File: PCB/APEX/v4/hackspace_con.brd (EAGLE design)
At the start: 73.7 x 26.7 mm, 13 parts

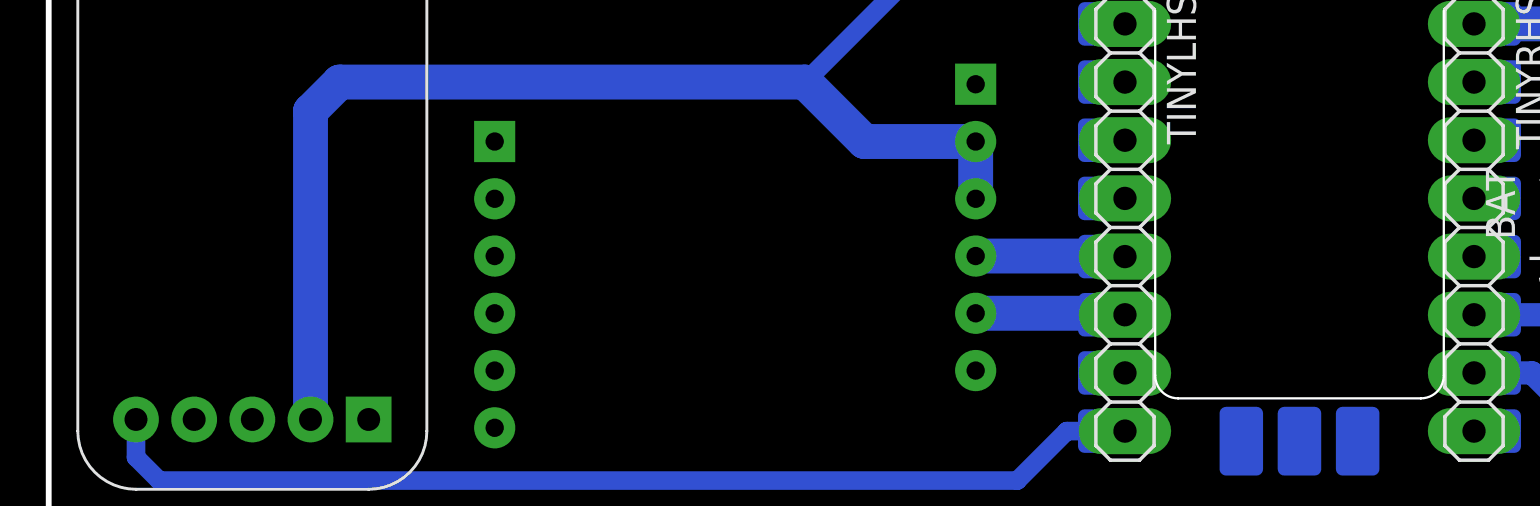
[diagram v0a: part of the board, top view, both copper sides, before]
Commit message: add labels
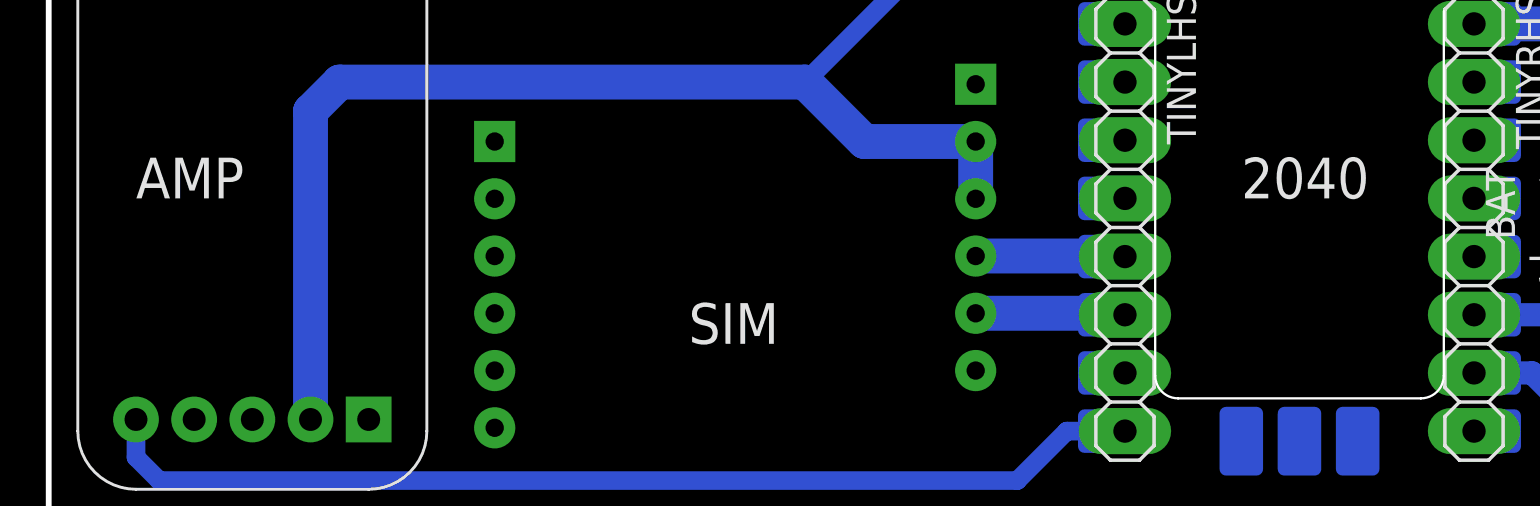
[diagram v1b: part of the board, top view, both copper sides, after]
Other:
- board text added: "2040"
- board text added: "AMP"
- board text added: "SIM"

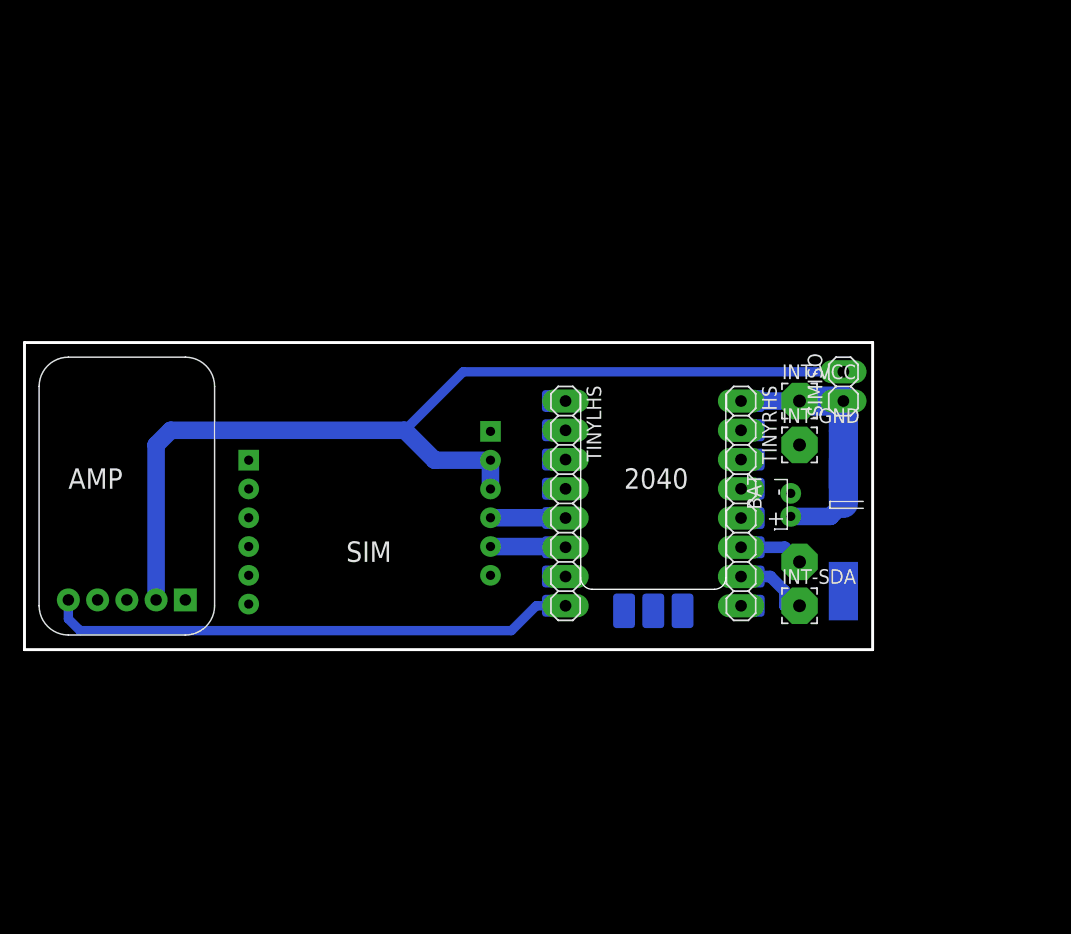
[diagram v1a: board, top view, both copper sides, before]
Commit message: flip installation orientation
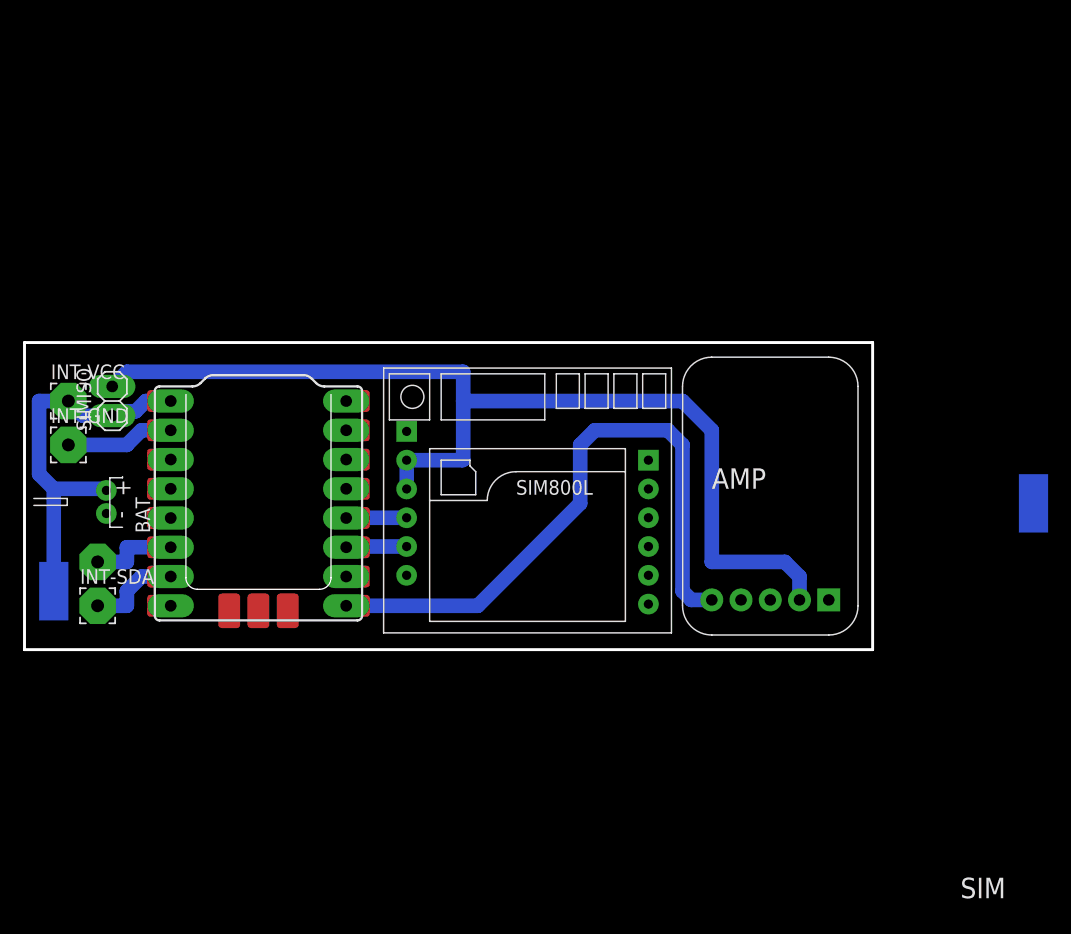
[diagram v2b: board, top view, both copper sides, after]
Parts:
- moved EXTV+ 69.5 mm to (-17.8, -52.1)
- moved SIMISO 63.5 mm to (-12.7, -35.6)
- moved INT-GND 63.5 mm to (-16.5, -39.4)
- moved INT-VCC 63.5 mm to (-16.5, -35.6)
- moved INT-SCL 61.0 mm to (-14.0, -49.5)
- moved INT-SDA 61.0 mm to (-14.0, -53.3)
- moved BAT 59.4 mm to (-13.2, -44.3), turned to 90 degrees
- moved JP2 55.9 mm to (44.5, -52.8)
- moved TINYRHS 49.5 mm to (-7.62, -44.5), flipped to the bottom
- moved A1 34.3 mm to (0.00, -34.3), flipped to the top
- moved TINYLHS 19.1 mm to (7.62, -44.5), flipped to the bottom
- moved EXTGND 18.2 mm to (67.3, -44.5)
- moved U$1 13.7 mm to (23.4, -44.2), flipped to the top
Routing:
- net VCC: track 19.7 -> 34.1 mm
- net GND: track 0.00 -> 9.42 mm
- net AIN+: track 45.6 -> 54.6 mm
- net SIMPOW: track 86.8 -> 90.3 mm
- net SCL: track 5.06 -> 7.62 mm
- net SDA: track 6.62 -> 8.15 mm
- net TX: track 5.99 -> 5.37 mm

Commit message: remove 2040 footprint
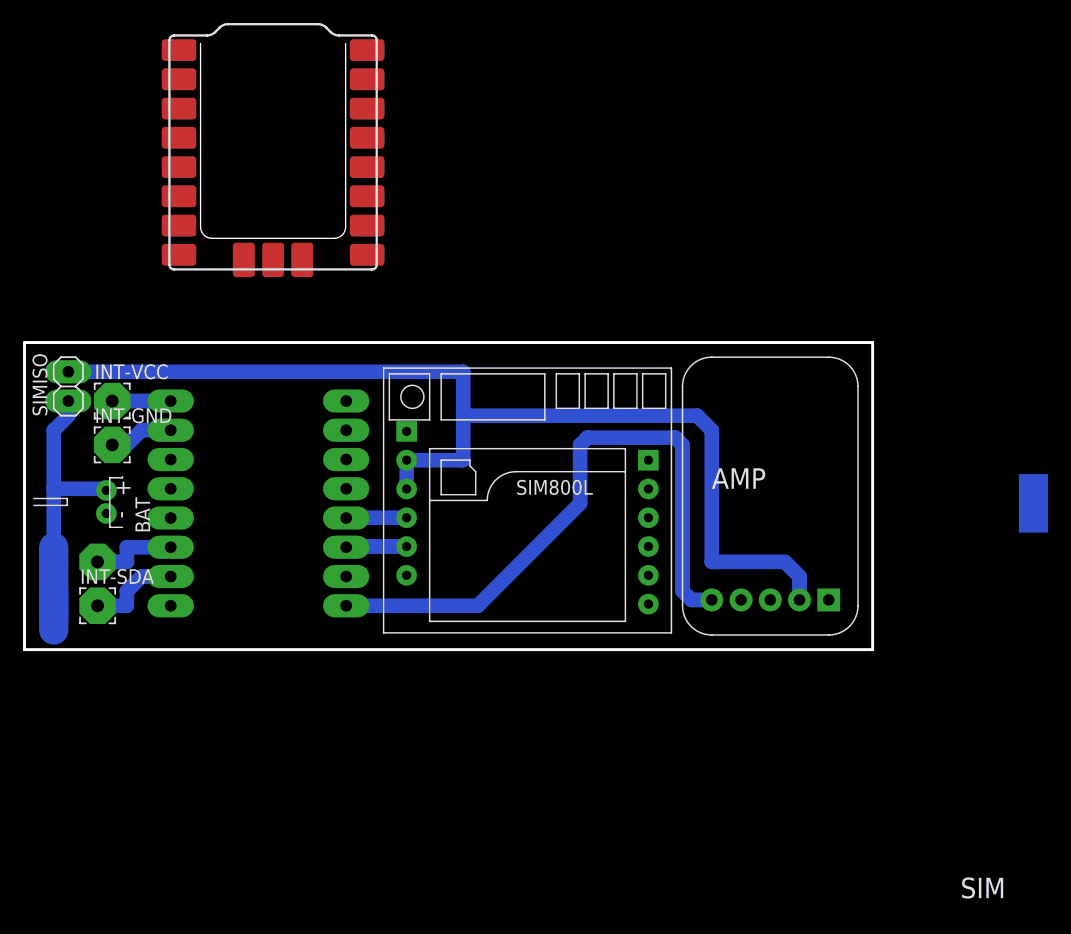
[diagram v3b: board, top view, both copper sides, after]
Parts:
- moved A1 30.5 mm to (1.27, -3.81)
- moved SIMISO 4.02 mm to (-16.5, -34.3)
- moved INT-GND 3.81 mm to (-12.7, -39.4)
- moved INT-VCC 3.81 mm to (-12.7, -35.6)
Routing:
- net GND: track 9.42 -> 4.34 mm
- net VCC: track 34.1 -> 30.1 mm
- net SIMPOW: track 90.3 -> 93.1 mm
- net AIN+: track 54.6 -> 54.1 mm

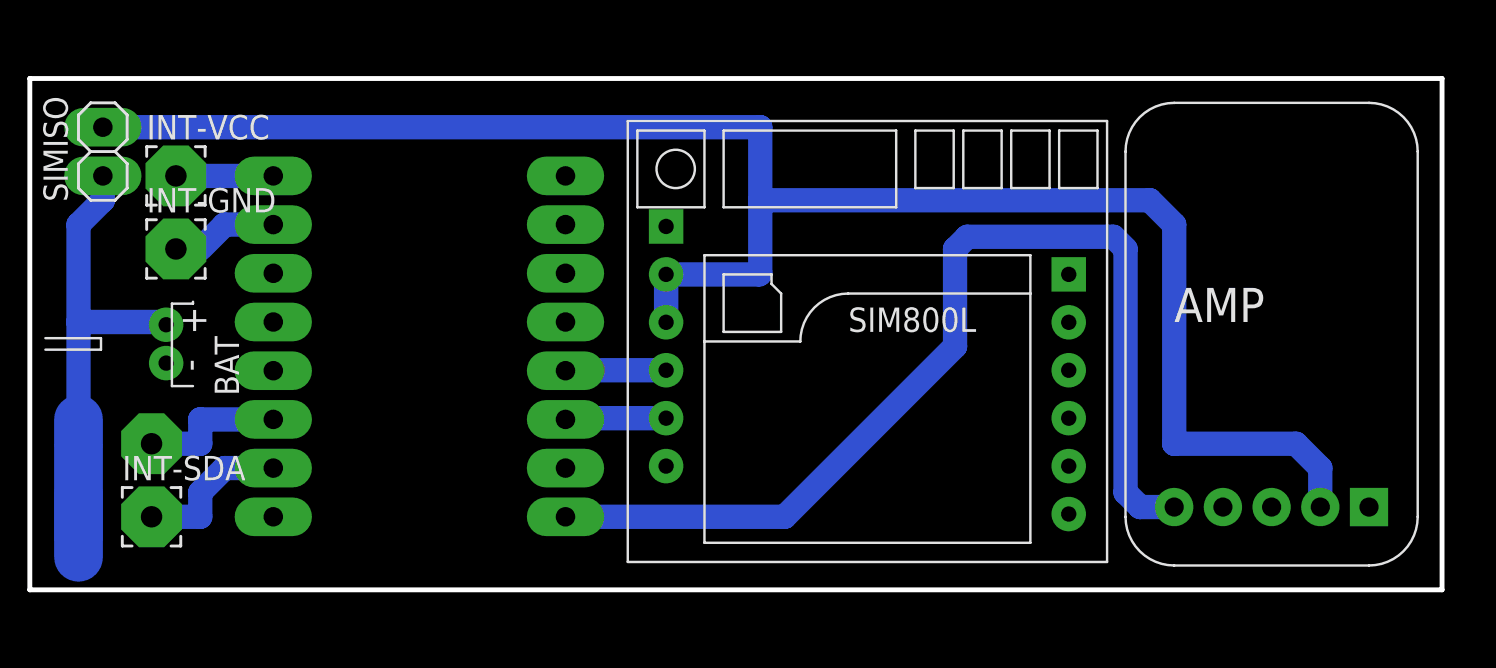
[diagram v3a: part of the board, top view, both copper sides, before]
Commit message: thiccer traces
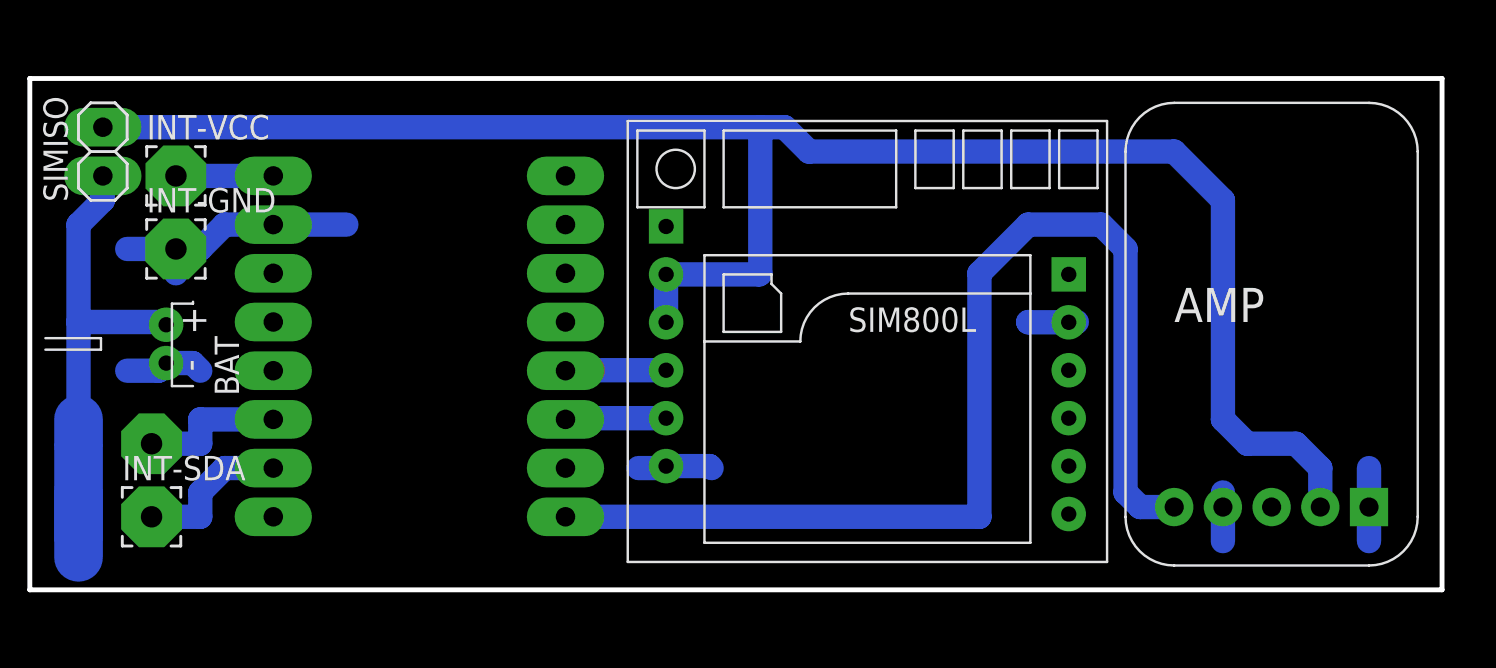
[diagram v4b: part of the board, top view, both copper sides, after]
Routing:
- net GND: track 4.34 -> 30.2 mm
- net AIN+: track 54.1 -> 59.0 mm
- net SIMPOW: track 93.1 -> 94.6 mm
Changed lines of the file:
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@@
 </polygon>
 <wire x1="-11.43" y1="-39.37" x2="-10.16" y2="-38.1" width="1.27" layer="16"/>
-<wire x1="-10.16" y1="-38.1" x2="-7.62" y2="-38.1" width="1.27" layer="16"/>
+<wire x1="41.91" y1="-52.07" x2="41.91" y2="-52.832" width="1.27" layer="16"/>
+<wire x1="41.91" y1="-52.832" x2="41.91" y2="-54.61" width="1.27" layer="16"/>
+<wire x1="49.53" y1="-50.8" x2="49.53" y2="-52.832" width="1.27" layer="16"/>
+<wire x1="49.53" y1="-52.832" x2="49.53" y2="-54.61" width="1.27" layer="16"/>
+<wire x1="12.868" y1="-50.696" x2="15.136" y2="-50.696" width="1.27" layer="16"/>
+<wire x1="15.136" y1="-50.696" x2="15.24" y2="-50.8" width="1.27" layer="16"/>
+<wire x1="12.868" y1="-50.696" x2="12.764" y2="-50.8" width="1.27" layer="16"/>
+<wire x1="12.764" y1="-50.8" x2="11.43" y2="-50.8" width="1.27" layer="16"/>
+<wire x1="-13.208" y1="-45.323" x2="-13.605" y2="-45.72" width="1.27" layer="16"/>
+<wire x1="-13.605" y1="-45.72" x2="-15.24" y2="-45.72" width="1.27" layer="16"/>
+<wire x1="-13.208" y1="-45.323" x2="-11.827" y2="-45.323" width="1.27" layer="16"/>
+<wire x1="-11.827" y1="-45.323" x2="-11.43" y2="-45.72" width="1.27" layer="16"/>
+<wire x1="-7.62" y1="-38.1" x2="-3.81" y2="-38.1" width="1.27" layer="16"/>
+<wire x1="-7.62" y1="-38.1" x2="-10.16" y2="-38.1" width="1.27" layer="16"/>
+<wire x1="-12.7" y1="-39.37" x2="-11.43" y2="-39.37" width="1.27" layer="16"/>
+<wire x1="-12.7" y1="-39.37" x2="-15.24" y2="-39.37" width="1.27" layer="16"/>
+<wire x1="-12.7" y1="-39.37" x2="-12.7" y2="-40.64" width="1.27" layer="16"/>
+<wire x1="33.868" y1="-43.196" x2="31.766" y2="-43.196" width="1.27" layer="16"/>
+<wire x1="31.766" y1="-43.196" x2="31.75" y2="-43.18" width="1.27" layer="16"/>
+<wire x1="33.868" y1="-43.196" x2="33.884" y2="-43.18" width="1.27" layer="16"/>
+<wire x1="33.884" y1="-43.18" x2="34.29" y2="-43.18" width="1.27" layer="16"/>
 <wire x1="1.27" y1="-23.3" x2="-6.9" y2="-22.86" width="0" layer="19" extent="1-1"/>
 <wire x1="-6.9" y1="-7.62" x2="-6.9" y2="-22.86" width="0" layer="19" extent="1-1"/>
 <wire x1="-7.62" y1="-38.1" x2="-6.9" y2="-22.86" width="0" layer="19" extent="1-1"/>
-<wire x1="67.31" y1="-44.45" x2="49.53" y2="-52.832" width="0" layer="19" extent="16-16"/>
-<wire x1="12.868" y1="-50.696" x2="-7.62" y2="-53.34" width="0" layer="19" extent="1-1"/>
+<wire x1="67.31" y1="-44.45" x2="49.53" y2="-50.8" width="0" layer="19" extent="16-16"/>
 </signal>
 <signal name="VCC">
@@
 <contactref element="U$1" pad="RST"/>
 <contactref element="JP2" pad="2"/>
-<wire x1="17.78" y1="-33.02" x2="17.78" y2="-36.83" width="1.27" layer="16"/>
-<wire x1="17.78" y1="-36.83" x2="17.78" y2="-40.64" width="1.27" layer="16"/>
+<wire x1="17.78" y1="-33.02" x2="17.78" y2="-40.64" width="1.27" layer="16"/>
 <wire x1="17.78" y1="-40.64" x2="17.724" y2="-40.696" width="1.27" layer="16"/>
 <wire x1="17.724" y1="-40.696" x2="12.868" y2="-40.696" width="1.27" layer="16"/>
 <wire x1="12.868" y1="-40.696" x2="12.868" y2="-43.196" width="1.27" layer="16"/>
+<wire x1="-16.51" y1="-33.02" x2="17.78" y2="-33.02" width="1.27" layer="16"/>
+<wire x1="17.78" y1="-33.02" x2="19.05" y2="-33.02" width="1.27" layer="16"/>
 <wire x1="46.99" y1="-52.832" x2="46.99" y2="-50.8" width="1.27" layer="16"/>
 <wire x1="46.99" y1="-50.8" x2="45.72" y2="-49.53" width="1.27" layer="16"/>
-<wire x1="45.72" y1="-49.53" x2="39.37" y2="-49.53" width="1.27" layer="16"/>
-<wire x1="39.37" y1="-49.53" x2="39.37" y2="-38.1" width="1.27" layer="16"/>
-<wire x1="39.37" y1="-38.1" x2="38.1" y2="-36.83" width="1.27" layer="16"/>
-<wire x1="38.1" y1="-36.83" x2="17.78" y2="-36.83" width="1.27" layer="16"/>
-<wire x1="-16.51" y1="-33.02" x2="17.78" y2="-33.02" width="1.27" layer="16"/>
+<wire x1="45.72" y1="-49.53" x2="43.18" y2="-49.53" width="1.27" layer="16"/>
+<wire x1="43.18" y1="-49.53" x2="41.91" y2="-48.26" width="1.27" layer="16"/>
+<wire x1="41.91" y1="-48.26" x2="41.91" y2="-36.83" width="1.27" layer="16"/>
+<wire x1="41.91" y1="-36.83" x2="39.37" y2="-34.29" width="1.27" layer="16"/>
+<wire x1="20.32" y1="-34.29" x2="19.05" y2="-33.02" width="1.27" layer="16"/>
+<wire x1="39.37" y1="-34.29" x2="20.32" y2="-34.29" width="1.27" layer="16"/>
 </signal>
 <signal name="AIN+">
@@
 <contactref element="A1" pad="7"/>
 <contactref element="TINYLHS" pad="8"/>
-<wire x1="27.94" y1="-44.45" x2="27.94" y2="-39.37" width="1.27" layer="16"/>
-<wire x1="27.94" y1="-44.45" x2="19.05" y2="-53.34" width="1.27" layer="16"/>
-<wire x1="19.05" y1="-53.34" x2="7.62" y2="-53.34" width="1.27" layer="16"/>
-<wire x1="27.94" y1="-39.37" x2="28.575" y2="-38.735" width="1.27" layer="16"/>
-<wire x1="28.575" y1="-38.735" x2="36.195" y2="-38.735" width="1.27" layer="16"/>
-<wire x1="36.195" y1="-38.735" x2="36.83" y2="-39.37" width="1.27" layer="16"/>
-<wire x1="36.83" y1="-52.07" x2="37.592" y2="-52.832" width="1.27" layer="16"/>
+<wire x1="37.592" y1="-52.832" x2="36.83" y2="-52.07" width="1.27" layer="16"/>
 <wire x1="37.592" y1="-52.832" x2="39.37" y2="-52.832" width="1.27" layer="16"/>
-<wire x1="36.83" y1="-39.37" x2="36.83" y2="-52.07" width="1.27" layer="16"/>
+<wire x1="36.83" y1="-52.07" x2="36.83" y2="-39.37" width="1.27" layer="16"/>
+<wire x1="36.83" y1="-39.37" x2="35.56" y2="-38.1" width="1.27" layer="16"/>
+<wire x1="31.75" y1="-38.1" x2="29.21" y2="-40.64" width="1.27" layer="16"/>
+<wire x1="29.21" y1="-40.64" x2="29.21" y2="-53.34" width="1.27" layer="16"/>
+<wire x1="35.56" y1="-38.1" x2="31.75" y2="-38.1" width="1.27" layer="16"/>
+<wire x1="29.21" y1="-53.34" x2="7.62" y2="-53.34" width="1.27" layer="16"/>
 <wire x1="7.62" y1="-53.34" x2="9.44" y2="-22.86" width="0" layer="19" extent="1-1"/>
 </signal>
